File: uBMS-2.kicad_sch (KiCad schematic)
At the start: 106 parts, among them J1 DX07S016JA1R1500, J2 XT60PW-M20, J3 XT60PW-M20, Q3 NTD5865NL, SW1 PTS815_SJK_250_SMTR_LFS, SW2 PTS815_SJK_250_SMTR_LFS, SW3 PTS815_SJK_250_SMTR_LFS, U1 LM5166X, U12 CP2102N-A02-GQFN24, U13 SN74HC595BRWNR, U14 SSM6N7002KFU, U15 SSM6N7002KFU, U16 SSM6N7002KFU, U17 SSM6N7002KFU, U18 SSM6N7002KFU, U2 ADS1115IDGS, U3 TLV1117-33, U4 TL431DBZ, U5 ESP32-WROOM-32, U6 TSC2012IDT, U7 SN74HC595BRWNR, U8 SN74HC595BRWNR, U9 VDMG10C0

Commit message: Updated schematic, added ESP32-S2
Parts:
- removed C7: 0.1uF, Capacitor_SMD:C_0805_2012Metric, symbol Device:C_Small
- removed C8: 1uF, Capacitor_SMD:C_0805_2012Metric, symbol Device:C_Small
- removed CIN1: 2.2uF, Capacitor_SMD:C_1206_3216Metric, symbol Device:C_Small
- removed COUT1: 47uF, Capacitor_SMD:C_1206_3216Metric, symbol Device:C_Small
- removed D2: 150060VS55040, LED_SMD:LED_0603_1608Metric_Castellated, symbol Device:LED
- removed D3: 150060SS55040, LED_SMD:LED_0603_1608Metric_Castellated, symbol Device:LED
- removed F1: 500mA PTC, ClementsFootprints:0ZCJ0050FF2G_3216X125N, symbol Device:Polyfuse
- removed H1, H2, H3, H4: MountingHole, MountingHole:MountingHole_2mm, symbol Mechanical:MountingHole
- removed L1: 100uH, ClementsFootprints:1267AY-101M=P3, symbol Device:L
- removed R100, R101, R102, R103, R104, R21, R6, R9, R93, R94, R95, R96, R97: 10k, Resistor_SMD:R_0603_1608Metric_Pad0.98x0.95mm_HandSolder, symbol Device:R
- removed R23: 71.5k, Resistor_SMD:R_0603_1608Metric_Pad0.98x0.95mm_HandSolder, symbol Device:R
- removed R24: 105k, Resistor_SMD:R_0603_1608Metric_Pad0.98x0.95mm_HandSolder, symbol Device:R
- removed R4: 330R, Resistor_SMD:R_0603_1608Metric_Pad0.98x0.95mm_HandSolder, symbol Device:R
- removed R5: 47R, Resistor_SMD:R_0603_1608Metric_Pad0.98x0.95mm_HandSolder, symbol Device:R
- removed R91, R92, R98, R99: 2.2k, Resistor_SMD:R_0603_1608Metric_Pad0.98x0.95mm_HandSolder, symbol Device:R
- removed U1: LM5166X, Package_SON:Texas_S-PVSON-N10_ThermalVias, symbol Regulator_Switching:LM5166X
- removed U12: CP2102N-A02-GQFN24, Package_DFN_QFN:QFN-24-1EP_4x4mm_P0.5mm_EP2.6x2.6mm, symbol ClementsSymbols:CP2102N-A02-GQFN24
- removed U14, U15, U16, U17, U18: SSM6N7002KFU, Package_TO_SOT_SMD:SOT-363_SC-70-6, symbol ClementsSymbols:SSM6N7002KFU
- removed U3: TLV1117-33, Package_TO_SOT_SMD:SOT-223-3_TabPin2, symbol Regulator_Linear:TLV1117-33
- removed U5: ESP32-WROOM-32, RF_Module:ESP32-WROOM-32, symbol RF_Module:ESP32-WROOM-32
- added C7, C8: 22pF, symbol Device:C
- added H1, H2, H3, H4: MountingHole_Pad, symbol Mechanical:MountingHole_Pad
- added U1: ESP32-S2-MINI-1, ClementsFootprints:ESP32-S2-MINI-1, symbol ClementsSymbols:ESP32-S2-MINI-1
- C5: value 33nF -> 10nF; footprint Capacitor_SMD:C_0805_2012Metric -> Capacitor_SMD:C_0402_1005Metric; Comment 0.033µF ±10% 50V Ceramic Capacitor X7R 0805 (2012 Metric) -> (none); Digikey Number 399-1165-2-ND -> (none); Part Number C0805C333K5RACTU -> (none); Price ($) 0.12 -> (none)
- C6: value 1uF -> 0.1uF; Comment 1µF -20%, +80% 16V Ceramic Capacitor Y5V (F) 0805 (2012 Met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 -> 0.1µF -20%, +80% 16V Ceramic Capacitor Y5V 0805 (2012 Metri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; Digikey Number 399-8011-2-ND -> 399-9159-2-ND; Part Number C0805C105Z4VACTU -> C0805C104Z4VACTU
- R2: value 47R -> 27R; footprint Resistor_SMD:R_0603_1608Metric_Pad0.98x0.95mm_HandSolder -> (none)
- R3: value 330R -> 27R; footprint Resistor_SMD:R_0603_1608Metric_Pad0.98x0.95mm_HandSolder -> (none)
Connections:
- net +3V3: now also C5.1, R1.1, U1.3 (3V3); no longer R3.1
- net +5V: no longer C6.1
- net BTN_1: now also U1.36 (IO40)
- net ESP_EN: now also R1.2, U1.45 (EN)
- net GND: now also C7.2, C8.2, H1.1, H2.1, H3.1, H4.1, U1.1 (GND), U1.2 (GND), U1.30 (GND), U1.42 (GND), U1.43 (GND), U1.46 (GND), U1.47 (GND), U1.48 (GND), U1.49 (GND), U1.50 (GND), U1.51 (GND), U1.52 (GND), U1.53 (GND), U1.54 (GND), U1.55 (GND), U1.56 (GND), U1.57 (GND), U1.58 (GND), U1.59 (GND), U1.60 (GND), U1.61 (GND), U1.62 (GND), U1.63 (GND), U1.64 (GND), U1.65 (GND), U1.66 (GND), U1.67 (GND), U1.68 (GND), U1.69 (GND), U1.70 (GND), U1.71 (GND), U1.72 (GND), U1.73 (GND); no longer R1.2
- net PWM_Blnce_1: now also U1.5 (IO1)
- net PWM_Blnce_10: now also U1.16 (IO12)
- net PWM_Blnce_11: now also U1.17 (IO13)
- net PWM_Blnce_12: now also U1.18 (IO14)
- net PWM_Blnce_2: now also U1.6 (IO2)
- net PWM_Blnce_3: now also U1.7 (IO3)
- net PWM_Blnce_4: now also U1.8 (IO4)
- net PWM_Blnce_5: now also U1.9 (IO5)
- net PWM_Blnce_6: now also U1.10 (IO6)
- net PWM_Blnce_7: now also U1.11 (IO7)
- net PWM_Blnce_8: now also U1.14 (IO10)
- net PWM_Blnce_9: now also U1.15 (IO11)
- net RCLK_3V3: now also U1.34 (IO38)
- net SCL_3V3: now also U1.13 (IO9)
- net SDA_3V3: now also U1.12 (IO8)
- net SER_3V3: now also U1.33 (IO37)
- net SRCLK_3V3: now also U1.32 (IO36)
- net UART_RX: now also U1.40 (RXD0)
- net UART_TX: now also U1.39 (TXD0)
- net USB_D+: now also R3.1, U1.24 (IO20); no longer J1.6 (D+), J1.7 (D+)
- net USB_D-: now also R2.1, U1.23 (IO19); no longer J1.5 (D-), J1.8 (D-)
- net VBUS_3V3: now also C6.1
- net ~{OE_3V3}: now also U1.35 (IO39)
- net ~{SRCLR_3V3}: now also U1.31 (IO35)
- net USB_D_UT+: now reaches R3.2
- net USB_D_UT+: now also J1.6 (D+), J1.7 (D+), C8.1
- net DTR renamed USB_D_UT-
- net USB_D_UT-: now also J1.5 (D-), J1.8 (D-), C7.1
- no-connect marks 21 -> 18
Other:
- added sheet Level Shifts (levelshifts.kicad_sch)
- added sheet Power (power.kicad_sch)
- note added: "ESP32-S2"
- note added: "IO26 Unavailable with PSRAM Variant"
- note added: "Power"
- note added: "Termination Near MCU"
- note removed: "3V3 Regulator"
- note removed: "Buck Converter Power Supply"
- note removed: "ESP32 w/ Automatic UART Programming"
- note removed: "I2C Level Shifter"
- note removed: "Shift Reg Shifter 1"
- note removed: "Shift Reg Shifter 2"
- note removed: "Shift Reg Shifter 3"
- note removed: "TLV1117LV (1A)"
- title: Micro BMS v2 -> Micro BMS
- moved on the sheet: C1, C10, C11, C2, C3, C38, C39, C4, C40, C9, D1, D21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

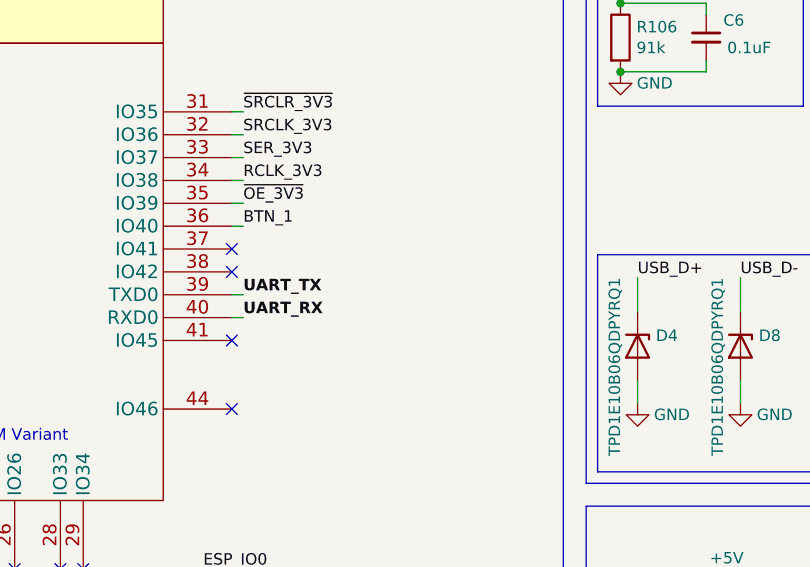
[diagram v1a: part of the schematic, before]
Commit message: Add test points
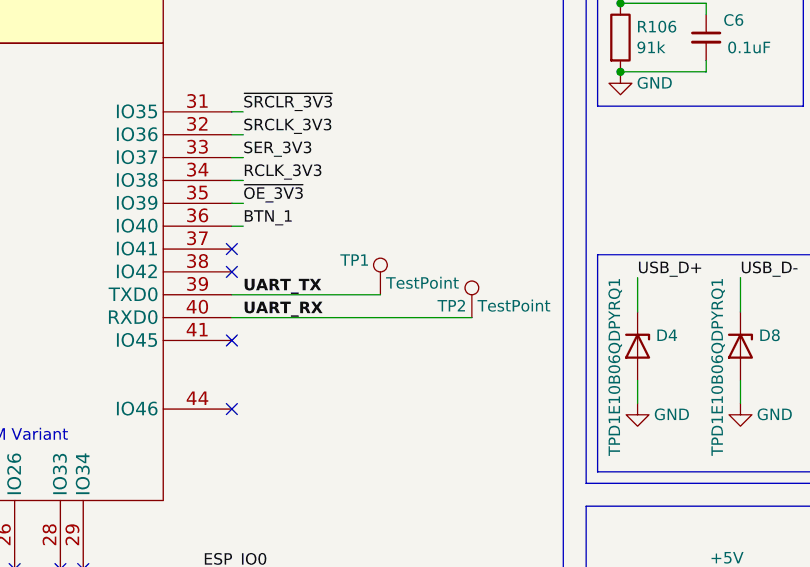
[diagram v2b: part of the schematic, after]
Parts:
- added TP1, TP2: TestPoint, symbol Connector:TestPoint
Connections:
- net UART_RX: now also TP2.1
- net UART_TX: now also TP1.1
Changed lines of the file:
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@@
     (stroke (width 0) (type default) (color 0 0 0 0))
   )
+  (wire (pts (xy 116.84 61.595) (xy 133.35 61.595))
+    (stroke (width 0) (type default) (color 0 0 0 0))
+  )
   (wire (pts (xy 60.96 114.3) (xy 63.5 114.3))
     (stroke (width 0) (type default) (color 0 0 0 0))
@@
     (stroke (width 0) (type default) (color 0 0 0 0))
   )
-  (wire (pts (xy 118.11 61.595) (xy 116.84 61.595))
-    (stroke (width 0) (type default) (color 0 0 0 0))
-  )
   (polyline (pts (xy 398.78 100.965) (xy 398.78 53.975))
     (stroke (width 0) (type default) (color 0 0 0 0))
@@
     (stroke (width 0) (type default) (color 0 0 0 0))
   )
-  (wire (pts (xy 118.11 64.135) (xy 116.84 64.135))
+  (wire (pts (xy 116.84 64.135) (xy 143.51 64.135))
     (stroke (width 0) (type default) (color 0 0 0 0))
   )
@@
     (pin "1")
   )
+  (symbol (lib_id "Connector:TestPoint") (at 133.35 61.595 0) (unit 1)
+    (in_bom yes) (on_board yes)
+    (property "Reference" "TP1" (id 0) (at 128.905 57.785 0)
+      (effects (font (size 1.27 1.27)) (justify left))
+    )
+    (property "Value" "TestPoint" (id 1) (at 133.985 60.325 0)
+      (effects (font (size 1.27 1.27)) (justify left))
+    )
+    (property "Footprint" "" (id 2) (at 138.43 61.595 0)
+      (effects (font (size 1.27 1.27)) hide)
+    )
+    (property "Datasheet" "~" (id 3) (at 138.43 61.595 0)
+      (effects (font (size 1.27 1.27)) hide)
+    )
+    (pin "1")
+  )
+  (symbol (lib_id "Connector:TestPoint") (at 143.51 64.135 0) (unit 1)
+    (in_bom yes) (on_board yes)
+    (property "Reference" "TP2" (id 0) (at 139.7 62.865 0)
+      (effects (font (size 1.27 1.27)) (justify left))
+    )
+    (property "Value" "TestPoint" (id 1) (at 144.145 62.865 0)
+      (effects (font (size 1.27 1.27)) (justify left))
+    )
+    (property "Footprint" "" (id 2) (at 148.59 64.135 0)
+      (effects (font (size 1.27 1.27)) hide)
+    )
+    (property "Datasheet" "~" (id 3) (at 148.59 64.135 0)
+      (effects (font (size 1.27 1.27)) hide)
+    )
+    (pin "1")
+  )
   (symbol (lib_id "Mechanical:MountingHole_Pad") (at 49.53 220.98 270) (unit 1)
     (in_bom yes) (on_board yes)
@@
       (reference "TH4") (unit 1) (value "10k") (footprint "Resistor_SMD:R_0201_0603Metric")
     )
+    (path "/b2af931e-13bc-4de5-9aaf-d25b595c04bc"
+      (reference "TP1") (unit 1) (value "TestPoint") (footprint "")
+    )
+    (path "/b6be73fc-d959-449a-a86c-8f74568c8753"
+      (reference "TP2") (unit 1) (value "TestPoint") (footprint "")
+    )
     (path "/691282b0-ca4e-4163-9504-4a978b77f0f2"

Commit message: More schematic updates
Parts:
- added D2: GREEN_LED, LED_SMD:LED_0603_1608Metric_Castellated, symbol Device:LED
- added R101: 1k, Resistor_SMD:R_0402_1005Metric, symbol Device:R
- added TP10, TP11, TP12, TP13, TP14, TP15, TP16, TP17, TP18, TP19, TP20, TP21, TP22, TP23, TP24, TP25, TP3, TP4, TP5, TP6, TP7, TP8, TP9: TestPoint, TestPoint:TestPoint_Pad_1.5x1.5mm, symbol Connector:TestPoint
- C1, C10, C11, C2, C3, C38, C39, C4, C40, C6, C9: footprint Capacitor_SMD:C_0805_2012Metric -> Capacitor_SMD:C_0402_1005Metric
- C7, C8: footprint (none) -> Capacitor_SMD:C_0402_1005Metric
- R10, R106, R11, R12, R13, R14, R15, R16, R17, R18, R19, R20, R22, R25, R26, R27, R28, R29, R30, R8, R88, R89, R90: footprint Resistor_SMD:R_0603_1608Metric_Pad0.98x0.95mm_HandSolder -> Resistor_SMD:R_0402_1005Metric
- TP1, TP2: footprint (none) -> TestPoint:TestPoint_Pad_1.5x1.5mm
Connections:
- net +3V3: now also TP25.1
- net +5V: now also TP23.1
- net ESP_EN: now also TP22.1
- net ESP_IO0: now also U1.4 (IO0), TP20.1
- net GND: now also D2.1 (K), TP17.1, TP19.1, TP21.1
- net MOD_DSC_G: now also U1.21 (IO17), TP24.1; no longer U8.15 (QA)
- net PWM_Blnce_1: now also TP4.1
- net PWM_Blnce_10: now also TP13.1
- net PWM_Blnce_11: now also TP14.1
- net PWM_Blnce_12: now also TP15.1
- net PWM_Blnce_2: now also TP5.1
- net PWM_Blnce_3: now also TP6.1
- net PWM_Blnce_4: now also TP7.1
- net PWM_Blnce_5: now also TP8.1
- net PWM_Blnce_6: now also TP9.1
- net PWM_Blnce_7: now also TP10.1
- net PWM_Blnce_8: now also TP11.1
- net PWM_Blnce_9: now also TP12.1
- net SCL_3V3: now also TP18.1
- net SDA_3V3: now also TP16.1
- net VBUS: now also R101.1
- net VBUS_3V3: now also U1.25 (IO21)
- net ADC_RDY_5V: now reaches U2.2 (ALERT/RDY)
- net ADC_RDY_3V3: now reaches U1.37 (IO41)
- net at U1.44 (IO46): now also TP3.1
- new net: D2.2 (A), R101.2
- no-connect marks 18 -> 13
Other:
- sheet Level Shifts ports: added ADC_RDY_3V3, ADC_RDY_5V; removed none
- note added: "Boot Button"
- note added: "Enable Button"
- note added: "GND Connections"
- note added: "Level Shifter"
- note added: "TSV"
- note added: "Test Points"
- moved on the sheet: C38, C39, C4, D22, D23, D24, D25, D5, D6, D7, H1, H2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

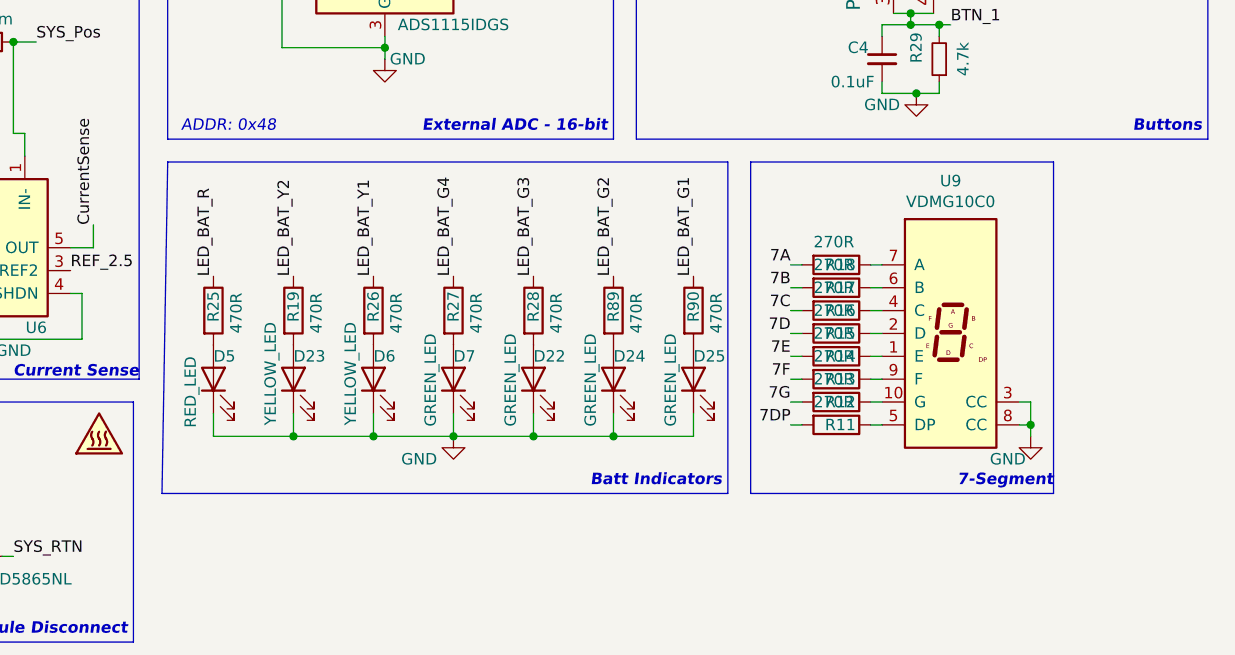
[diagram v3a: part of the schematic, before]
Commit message: Updated all of component values
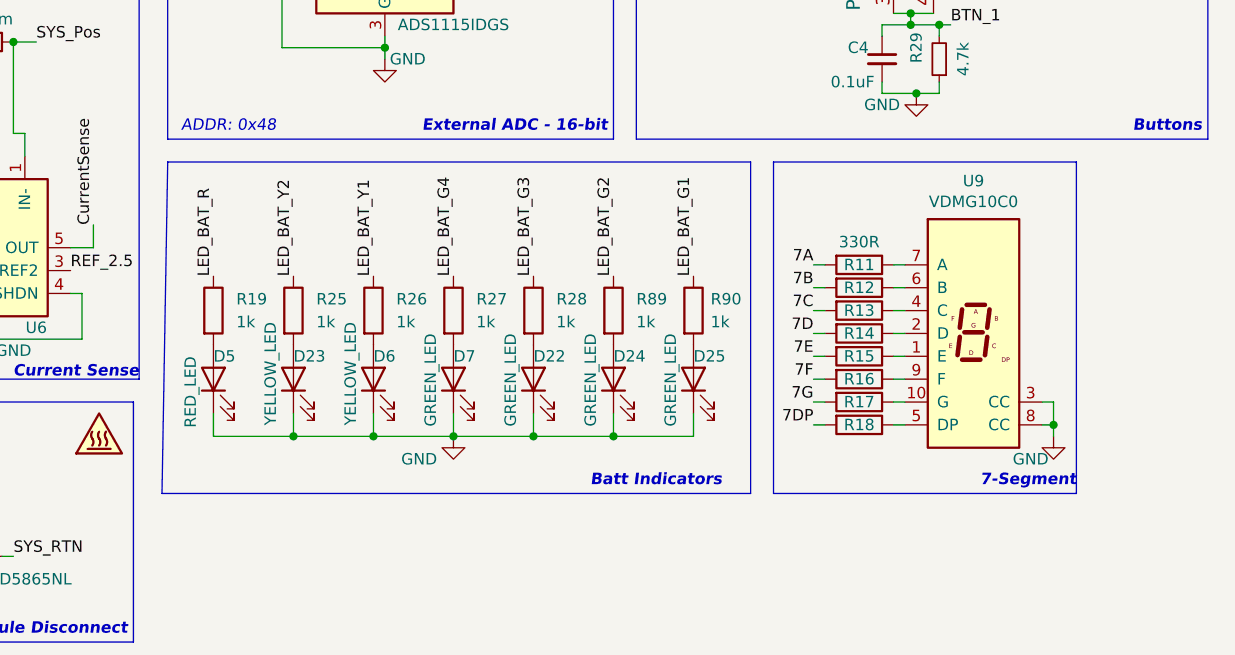
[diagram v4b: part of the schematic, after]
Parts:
- C1, C10, C11, C3, C38, C39, C4, C40, C6, C9: Comment 0.1µF -20%, +80% 16V Ceramic Capacitor Y5V 0805 (2012 Metri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 -> 0.1 µF ±10% 16V Ceramic Capacitor X7R 0402 (1005 Metric); Digikey Number 399-9159-2-ND -> 311-1338-1-ND; Part Number C0805C104Z4VACTU -> CC0402KRX7R7BB104; Price ($) 0.11 -> 0.1
- C2: footprint Capacitor_SMD:C_0402_1005Metric -> Capacitor_SMD:C_0805_2012Metric
- C5: Comment (none) -> 10000 pF ±10% 50V Ceramic Capacitor X7R 0402 (1005 Metric); Digikey Number (none) -> 490-4762-1-ND; Part Number (none) -> GCM155R71H103KA55D; Price ($) (none) -> 0.1
- C7, C8: Comment (none) -> 22 pF ±5% 50V Ceramic Capacitor C0G, NP0 0402 (1005 Metric); Digikey Number (none) -> 490-5868-1-ND; Part Number (none) -> GRM1555C1H220JA01D; Price ($) (none) -> 0.1
- H1, H2, H3, H4: footprint (none) -> MountingHole:MountingHole_2.5mm_Pad_TopBottom
- R1: footprint Resistor_SMD:R_0603_1608Metric_Pad0.98x0.95mm_HandSolder -> Resistor_SMD:R_0402_1005Metric; Comment (none) -> 10 kOhms ±1% 0.063W, 1/16W Chip Resistor 0402 (1005 Metric)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; Digikey Number (none) -> 311-10.0KLRCT-ND; Part Number (none) -> RC0402FR-0710KL; Price ($) (none) -> 0.1
- R10: Comment (none) -> 330 Ohms ±1% 0.063W, 1/16W Chip Resistor 0402 (1005 Metric)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; Digikey Number (none) -> 311-330LRCT-ND; Part Number (none) -> RC0402FR-07330RL; Price ($) (none) -> 0.1
- R101: Comment (none) -> 1 kOhms ±1% 0.063W, 1/16W Chip Resistor 0402 (1005 Metric) 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; Digikey Number (none) -> 311-1.00KLRCT-ND; Part Number (none) -> RC0402FR-071KL; Price ($) (none) -> 0.1
- R106: Comment (none) -> 91 kOhms ±1% 0.063W, 1/16W Chip Resistor 0402 (1005 Metric)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; Digikey Number (none) -> 311-91.0KLRCT-ND; Part Number (none) -> RC0402FR-0791KL; Price ($) (none) -> 0.1
- R11, R12, R13, R14, R15, R16, R17, R18: value 270R -> 330R; Comment (none) -> 330 Ohms ±1% 0.063W, 1/16W Chip Resistor 0402 (1005 Metric)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; Digikey Number (none) -> 311-330LRCT-ND; Part Number (none) -> RC0402FR-07330RL; Price ($) (none) -> 0.1
- R19, R25, R26, R27, R28, R89, R90: value 470R -> 1k; Comment (none) -> 1 kOhms ±1% 0.063W, 1/16W Chip Resistor 0402 (1005 Metric) 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; Digikey Number (none) -> 311-1.00KLRCT-ND; Part Number (none) -> RC0402FR-071KL; Price ($) (none) -> 0.1
- R2, R3: footprint (none) -> Resistor_SMD:R_0402_1005Metric; Comment (none) -> 27 Ohms ±1% 0.063W, 1/16W Chip Resistor 0402 (1005 Metric) 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; Digikey Number (none) -> YAG3086CT-ND; Part Number (none) -> RC0402FR-0727RL; Price ($) (none) -> 0.1
- R20, R29: Comment (none) -> 4.7 kOhms ±1% 0.063W, 1/16W Chip Resistor 0402 (1005 Metric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; Digikey Number (none) -> 311-4.7KLRCT-ND; Part Number (none) -> RC0402FR-074K7L; Price ($) (none) -> 0.1
- R22: Comment (none) -> 47 kOhms ±1% 0.063W, 1/16W Chip Resistor 0402 (1005 Metric)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; Digikey Number (none) -> 311-47.0KLRCT-ND; Part Number (none) -> RC0402FR-0747KL; Price ($) (none) -> 0.1
- R30, R88: Comment (none) -> 5.1 kOhms ±1% 0.063W, 1/16W Chip Resistor 0402 (1005 Metric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; Digikey Number (none) -> 311-5.10KLRCT-ND; Part Number (none) -> RC0402FR-075K1L; Price ($) (none) -> 0.1
- R8: Comment (none) -> 470 Ohms ±1% 0.063W, 1/16W Chip Resistor 0402 (1005 Metric)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; Digikey Number (none) -> 311-470LRCT-ND; Part Number (none) -> RC0402FR-07470RL; Price ($) (none) -> 0.1
- TP1, TP10, TP11, TP12, TP13, TP14, TP15, TP16, TP17, TP18, TP19, TP2, TP20, TP21, TP22, TP23, TP24, TP25, TP3, TP4, TP5, TP6, TP7, TP8, TP9: footprint TestPoint:TestPoint_Pad_1.5x1.5mm -> TestPoint:TestPoint_Pad_1.0x1.0mm
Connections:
- net 7A: now also R11.2; no longer R18.2
- net 7B: now also R12.2; no longer R17.2
- net 7C: now also R13.2; no longer R16.2
- net 7D: now also R14.2; no longer R15.2
- net 7DP: now also R18.2; no longer R11.2
- net 7E: now also R15.2; no longer R14.2
- net 7F: now also R16.2; no longer R13.2
- net 7G: now also R17.2; no longer R12.2
- net LED_BAT_R: now also R19.1; no longer R25.1
- net LED_BAT_Y2: now also R25.1; no longer R19.1
- net at U9.1 (E): now also R15.1; no longer R14.1
- net at U9.10 (G): now also R17.1; no longer R12.1
- net at U9.2 (D): now also R14.1; no longer R15.1
- net at U9.4 (C): now also R13.1; no longer R16.1
- net at U9.5 (DP): now also R18.1; no longer R11.1
- net at U9.6 (B): now also R12.1; no longer R17.1
- net at U9.7 (A): now also R11.1; no longer R18.1
- net at U9.9 (F): now also R16.1; no longer R13.1
- net at D5.2 (A): now also R19.2; no longer R25.2
- net at D23.2 (A): now also R25.2; no longer R19.2
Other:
- moved on the sheet: U9

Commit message: DCDC Section Mostly complete
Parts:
- added C50: 1uF, Capacitor_SMD:C_0805_2012Metric, symbol Device:C_Small
- D2, D22, D23, D24, D25, D5, D6, D7: footprint LED_SMD:LED_0603_1608Metric_Castellated -> LED_SMD:LED_0603_1608Metric
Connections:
- net GND: now also C50.2
- net USB_D+: no longer D4.1 (K)
- net USB_D-: no longer D8.1 (K)
- net USB_D_UT+: now also D4.1 (K)
- net USB_D_UT-: now also D8.1 (K)
- net VBUS: now also C50.1
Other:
- moved on the sheet: D2, D21, D8, R101

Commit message: More Layout!
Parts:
- added TP26: TestPoint, TestPoint:TestPoint_Pad_1.0x1.0mm, symbol Connector:TestPoint
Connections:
- net TMUX_EN: now reaches U1.19 (IO15)
- net VMUX_EN: now reaches U1.20 (IO16)
- net at U1.41 (IO45): now also TP26.1
- no-connect marks 13 -> 10

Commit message: More Layout
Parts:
- TP1, TP10, TP11, TP12, TP13, TP14, TP15, TP16, TP17, TP18, TP19, TP2, TP20, TP21, TP22, TP23, TP24, TP25, TP26, TP3, TP4, TP5, TP6, TP7, TP8, TP9: footprint TestPoint:TestPoint_Pad_1.0x1.0mm -> TestPoint:TestPoint_Pad_D1.0mm
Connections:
- net PWM_Blnce_10: now also U1.18 (IO14); no longer U1.16 (IO12)
- net PWM_Blnce_12: now also U1.16 (IO12); no longer U1.18 (IO14)
- net PWM_Blnce_7: now also U1.15 (IO11); no longer U1.11 (IO7)
- net PWM_Blnce_9: now also U1.11 (IO7); no longer U1.15 (IO11)

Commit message: More updates!
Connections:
- net 7A: now also U7.7 (QH); no longer U7.15 (QA)
- net 7B: now also U7.15 (QA); no longer U7.7 (QH)
- net 7F: now also U7.6 (QG); no longer U7.5 (QF)
- net 7G: now also U7.5 (QF); no longer U7.6 (QG)
- net S0_T: now also U13.1 (QB); no longer U13.15 (QA)
- net S0_V: now also U13.7 (QH); no longer U13.4 (QE)
- net S1_T: now also U13.15 (QA); no longer U13.1 (QB)
- net S1_V: now also U13.6 (QG); no longer U13.5 (QF)
- net S2_V: now also U13.4 (QE); no longer U13.6 (QG)
- net S3_V: now also U13.5 (QF); no longer U13.7 (QH)
